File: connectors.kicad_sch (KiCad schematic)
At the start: 4 parts, among them J1 Conn_01x04_Pin, J2 Conn_01x09_Pin, J3 Conn_01x04_Pin, J4 Conn_02x03_Odd_Even

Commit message: Fixed outstanding issues
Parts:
- renumbered J2 to J1, J1 to J2
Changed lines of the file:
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@@
 		(on_board yes)
 		(dnp no)
-		(property "Reference" "J1"
+		(property "Reference" "J2"
 			(at 46.355 40.64 0)
 			(effects
@@
 		)
 		(pin "2"
+		)
+		(instances
+			(project "project4_mcu_datalogger"
+				(path "/6791cede-e2c8-424a-b751-f1a182bcbb22/14841377-e15c-47f6-9750-1c87c8194bca"
+					(reference "J2")
+					(unit 1)
+				)
+			)
 		)
 	)
@@
 		(pin "2"
 		)
+		(instances
+			(project "project4_mcu_datalogger"
+				(path "/6791cede-e2c8-424a-b751-f1a182bcbb22/14841377-e15c-47f6-9750-1c87c8194bca"
+					(reference "J4")
+					(unit 1)
+				)
+			)
+		)
 	)
 	(symbol
@@
 		(on_board yes)
 		(dnp no)
-		(property "Reference" "J2"
+		(property "Reference" "J1"
 			(at 45.085 60.96 0)
 			(effects
@@
 		(pin "1"
 		)
+		(instances
+			(project "project4_mcu_datalogger"
+				(path "/6791cede-e2c8-424a-b751-f1a182bcbb22/14841377-e15c-47f6-9750-1c87c8194bca"
+					(reference "J1")
+					(unit 1)
+				)
+			)
+		)
 	)

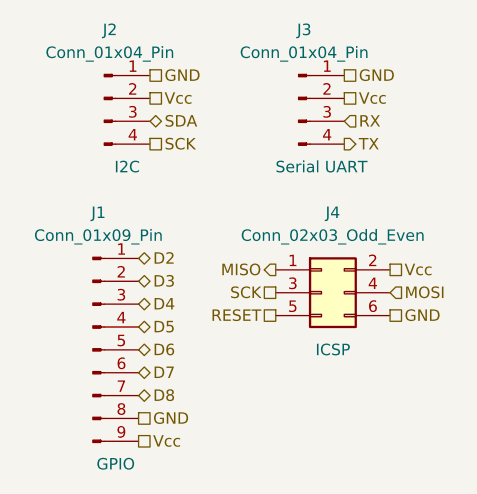
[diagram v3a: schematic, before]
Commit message: Fixed two defects in the schematic
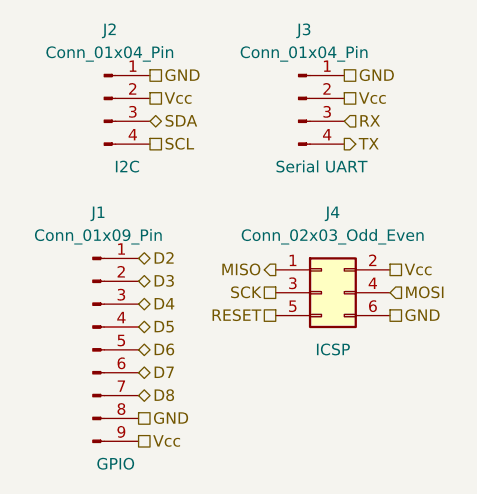
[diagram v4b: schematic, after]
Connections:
- net SCK: no longer J2.4 (Pin_4)
- new net SCL: J2.4 (Pin_4)
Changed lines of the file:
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@@
 		)
 	)
-	(hierarchical_label "SCK"
+	(hierarchical_label "SCL"
 		(shape passive)
 		(at 50.8 53.34 0)
